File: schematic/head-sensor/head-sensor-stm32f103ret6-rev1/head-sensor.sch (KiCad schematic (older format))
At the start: 11 parts

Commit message: Head sensor schematic in process
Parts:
- added P?: USART1, ~, symbol CONN_4
- added P?: NRF24L01, ~, symbol NRF24L01
- added P?: RFID-RC522-MODULE, ~, symbol RFID-RC522-MODULE
- added P? (x3): CONN_1, ~, symbol CONN_1
- added P?: USART3, ~, symbol CONN_4
- added P?: SensorsIn, ~, symbol CONN_6
- added Q? (x3): MOSFET_N, ~, symbol MOSFET_N
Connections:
- net +3.3V: now also P?.2 (P2), P?.2 (VCC), P?.7 (RST), P?.8 (3.3V)
- net DGND: now also P?.1 (GND), P?.1 (P1), P?.1 (P1), P?.6 (GND)
- net at U?.14 (WKUP/USART2_CTS/ADC123_IN0/TIM2_CH1_ETR/TIM5_CH1/TIM8_ETR/PA0): now also P?.1
- net at U?.15 (USART2_RTS/ADC123_IN1/TIM5_CH2/TIM2_CH2/PA1): now also P?.2
- net at U?.16 (USART2_TX/TIM5_CH3/ADC123_IN2/TIM2_CH3/PA2): now also P?.3
- net at U?.17 (USART2_RX/TIM5_CH4/ADC123_IN3/TIM2_CH4/PA3): now also P?.4
- net at U?.20 (SPI1_NSS/USART2_CK/DAC_OUT1/ADC12_IN4/PA4): now also P?.5
- net at U?.21 (SPI1_SCK/DAC_OUT2/ADC12_IN5/PA5): now also P?.6
- net at U?.22 (SPI1_MISO/TIM8_BKIN/ADC12_IN6/TIM3_CH1/PA6): now also Q?.G
- net at U?.23 (SPI1_MOSI/TIM8_CH1N/ADC12_IN7/TIM3_CH2/PA7): now also Q?.G
- net at U?.26 (ADC12_IN8/TIM3_CH3/TIM8_CH2N/PB0): now also Q?.G
- net at U?.29 (I2C2_SCL/USART3_TX/PB10): now also P?.3 (P3)
- net at U?.30 (I2C2_SDA/USART3_RX/PB11): now also P?.4 (P4)
- net at U?.33 (SPI2_NSS/I2S2_WS/I2C2_SMBA/USART3_CK/TIM1_BKIN/PB12): now also P?.4 (CSN)
- net at U?.34 (SPI2_SCK/I2S2_CK/USART3_CTS/TIM1_CH1N/PB13): now also P?.5 (SCK)
- net at U?.35 (SPI2_MISO/TIM1_CH2N/USART3_RTS/PB14): now also P?.7 (MISO)
- net at U?.36 (SPI2_MOSI/I2S2_SD/TIM1_CH3N/PB15): now also P?.6 (MOSI)
- net at U?.42 (USART1_TX/TIM1_CH2/PA9): now also P?.3 (P3)
- net at U?.43 (USART1_RX/TIM1_CH3/PA10): now also P?.4 (P4)
- net at U?.46 (JTMS/SWDIO/PA13): now also P?.1
- net at U?.49 (JTCK/SWCLK/PA14): now also P?.1
- net at U?.50 (JTDI/SPI3_NSS/I2S3_WS/PA15): now also P?.1 (SDA)
- net at U?.55 (JTDO/SPI3_SCK/I2S3_CK/PB3): now also P?.2 (SCK)
- net at U?.56 (NJTRST/SPI3_MISO/PB4): now also P?.4 (MISO)
- net at U?.57 (I2C1_SMBA/SPI3_MOSI/I2S3_CD/PB5): now also P?.3 (MOSI)
- net at U?.58 (I2C1_SCL/TIM4_CH1/PB6): now also P?.5 (IRQ)
- net at U?.59 (I2C1_SDA/TIM4_CH2/PB7): now also P?.3 (CE)
- net at U?.61 (TIM4_CH3/SDIO_D4/PB8): now also P?.8 (IRQ)
- net at U?.7 (~NRST): now also P?.1
- new net AGND: Q?.S, Q?.S, Q?.S

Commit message: Head sensor schematic in process
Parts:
- added C?: C, ~, symbol C
- added P?: MICROSD-SDIO, ~, symbol MICROSD-SDIO
- added P?: CONN_4, ~, symbol CONN_4
- added P?: CONN_6, ~, symbol CONN_6
- added Q? (x6): MOSFET_N, ~, symbol MOSFET_N
- added R? (x8): R, ~, symbol R
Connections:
- net DGND is gone; now on net AGND: C?.2, C?.2, C?.2, C?.2, C?.2, C?.2, C?.2, P?.1 (GND), P?.1 (P1), P?.1 (P1), P?.6 (GND), U?.12 (VSSA), U?.18 (VSS), U?.31 (VSS), U?.47 (VSS), U?.63 (VSS)
- net GND is gone; now on net AGND: C?.2, U?.1 (GND/Adj)
- net +3.3V: now also C?.2, P?.4 (Vdd), R?.1, R?.2, R?.2, R?.2, R?.2
- net AGND: now also C?.1, P?.6 (GND), Q?.S, Q?.S, Q?.S, Q?.S, Q?.S, Q?.S
- net at U?.10 (PC2/ADC123_IN12): now also Q?.G
- net at U?.11 (PC3/ADC123_IN13): now also Q?.G
- net at U?.24 (PC4/ADC12_IN14): now also Q?.G
- net at U?.25 (PC5/ADC12_IN15): now also Q?.G
- net at U?.39 (PC8/TIM8_CH3/SDIO_D0): now also P?.7 (DAT0), R?.1
- net at U?.40 (PC9/TIM8_CH4/SDIO_D1): now also P?.8 (DAT1/nIRQ), R?.1
- net at U?.51 (PC10/UART4_TX/SDIO_D2): now also P?.1 (DAT2), R?.1
- net at U?.52 (PC11/UART4_RX/SDIO_D3): now also P?.2 (DAT3), R?.1
- net at U?.53 (PC12/UART5_TX/SDIO_CK): now also P?.5 (CLK)
- net at U?.54 (PD2/TIM3_ETR/UART5_RX/SDIO_CMD): now also P?.3 (CMD), R?.2
- net at U?.8 (PC0/ADC123_IN10): now also Q?.G
- net at U?.9 (PC1/ADC123_IN11): now also Q?.G
- net +BATT: now reaches U?.3 (In)
- net at Q?.D: now also R?.1 (x3)
- new net: P?.3 (P3), R?.2
- new net: P?.2 (P2), R?.2
- new net: P?.1 (P1), R?.2
- new net: P?.5, Q?.D
- new net: P?.4, Q?.D
- new net: P?.3, Q?.D
- new net: P?.2, Q?.D
- new net: P?.1, Q?.D
- new net: P?.6, Q?.D
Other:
- moved on the sheet: C?, U?

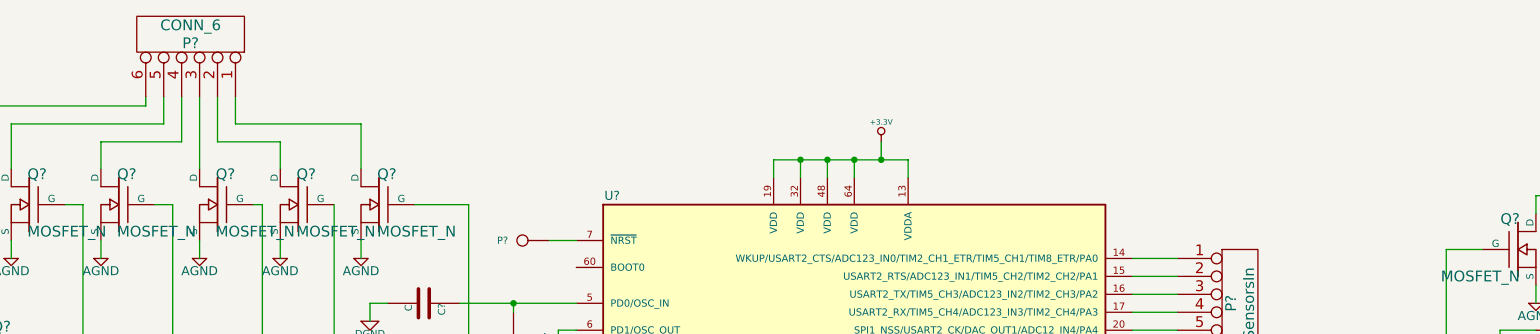
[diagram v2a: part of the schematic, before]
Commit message: Some connectors on scheme
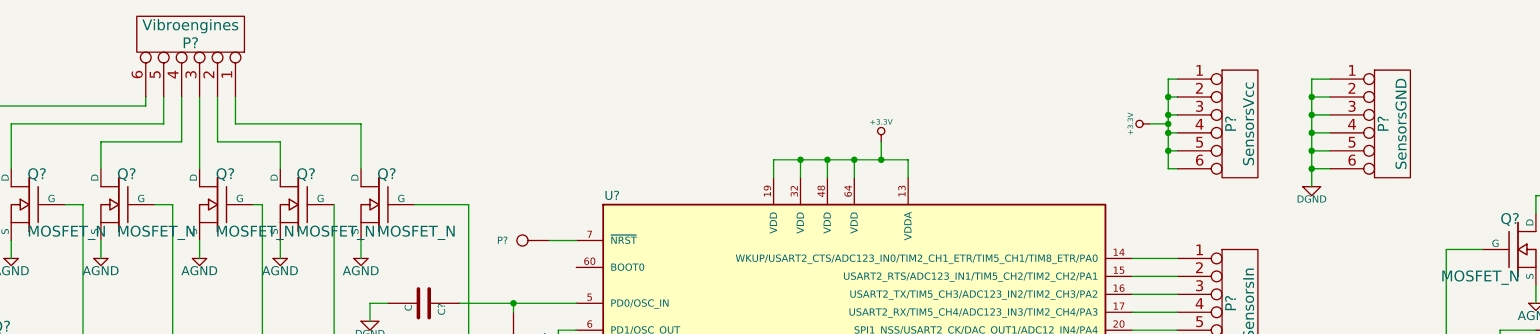
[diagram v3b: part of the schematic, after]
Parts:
- added P?: SensorsVcc, ~, symbol CONN_6
- added P?: SensorsGND, ~, symbol CONN_6
- P?: value CONN_6 -> Vibroengines
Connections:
- net +3.3V: now also P?.1, P?.2, P?.3, P?.4, P?.5, P?.6
- net AGND: now also P?.1, P?.2, P?.3, P?.4, P?.5, P?.6
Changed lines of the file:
@@
 Sheet 1 1
 Title "Lazertag head sensor"
-Date "13 jan 2015"
+Date "14 jan 2015"
 Rev "1"
 Comp ""
@@
 P 1900 700
 F 0 "P?" V 1850 700 60  0000 C CNN
-F 1 "CONN_6" V 1950 700 60  0000 C CNN
+F 1 "Vibroengines" V 1950 700 60  0000 C CNN
 F 2 "~" H 1900 700 60  0000 C CNN
 F 3 "~" H 1900 700 60  0000 C CNN
@@
 	2000 5300 2000 5400
 Connection ~ 2000 5400
+$Comp
+L CONN_6 P?
+U 1 1 54B638F6
+P 7750 1200
+F 0 "P?" V 7700 1200 60  0000 C CNN
+F 1 "SensorsVcc" V 7800 1200 60  0000 C CNN
+F 2 "~" H 7750 1200 60  0000 C CNN
+F 3 "~" H 7750 1200 60  0000 C CNN
+	1    7750 1200
+	1    0    0    -1
+$EndComp
+$Comp
+L CONN_6 P?
+U 1 1 54B63911
+P 8600 1200
+F 0 "P?" V 8550 1200 60  0000 C CNN
+F 1 "SensorsGND" V 8650 1200 60  0000 C CNN
+F 2 "~" H 8600 1200 60  0000 C CNN
+F 3 "~" H 8600 1200 60  0000 C CNN
+	1    8600 1200
+	1    0    0    -1
+$EndComp
+$Comp
+L +3.3V #PWR?
+U 1 1 54B63936
+P 7250 1200
+F 0 "#PWR?" H 7250 1160 30  0001 C CNN
+F 1 "+3.3V" H 7250 1310 30  0000 C CNN
+F 2 "" H 7250 1200 60  0000 C CNN
+F 3 "" H 7250 1200 60  0000 C CNN
+	1    7250 1200
+	0    -1   -1   0
+$EndComp
+Wire Wire Line
+	7400 1450 7350 1450
+Wire Wire Line
+	7350 1450 7350 950
+Wire Wire Line
+	7350 950  7400 950
+Wire Wire Line
+	7400 1050 7350 1050
+Connection ~ 7350 1050
+Wire Wire Line
+	7400 1150 7350 1150
+Connection ~ 7350 1150
+Wire Wire Line
+	7400 1250 7350 1250
+Connection ~ 7350 1250
+Wire Wire Line
+	7400 1350 7350 1350
+Connection ~ 7350 1350
+Wire Wire Line
+	7250 1200 7350 1200
+Connection ~ 7350 1200
+$Comp
+L DGND #PWR?
+U 1 1 54B63F33
+P 8150 1550
+F 0 "#PWR?" H 8150 1550 40  0001 C CNN
+F 1 "DGND" H 8150 1480 40  0000 C CNN
+F 2 "" H 8150 1550 60  0000 C CNN
+F 3 "" H 8150 1550 60  0000 C CNN
+	1    8150 1550
+	1    0    0    -1
+$EndComp
+Wire Wire Line
+	8150 1550 8150 950
+Wire Wire Line
+	8150 950  8250 950
+Wire Wire Line
+	8250 1050 8150 1050
+Connection ~ 8150 1050
+Wire Wire Line
+	8250 1150 8150 1150
+Connection ~ 8150 1150
+Wire Wire Line
+	8250 1250 8150 1250
+Connection ~ 8150 1250
+Wire Wire Line
+	8250 1350 8150 1350
+Connection ~ 8150 1350
+Wire Wire Line
+	8250 1450 8150 1450
+Connection ~ 8150 1450
 $EndSCHEMATC

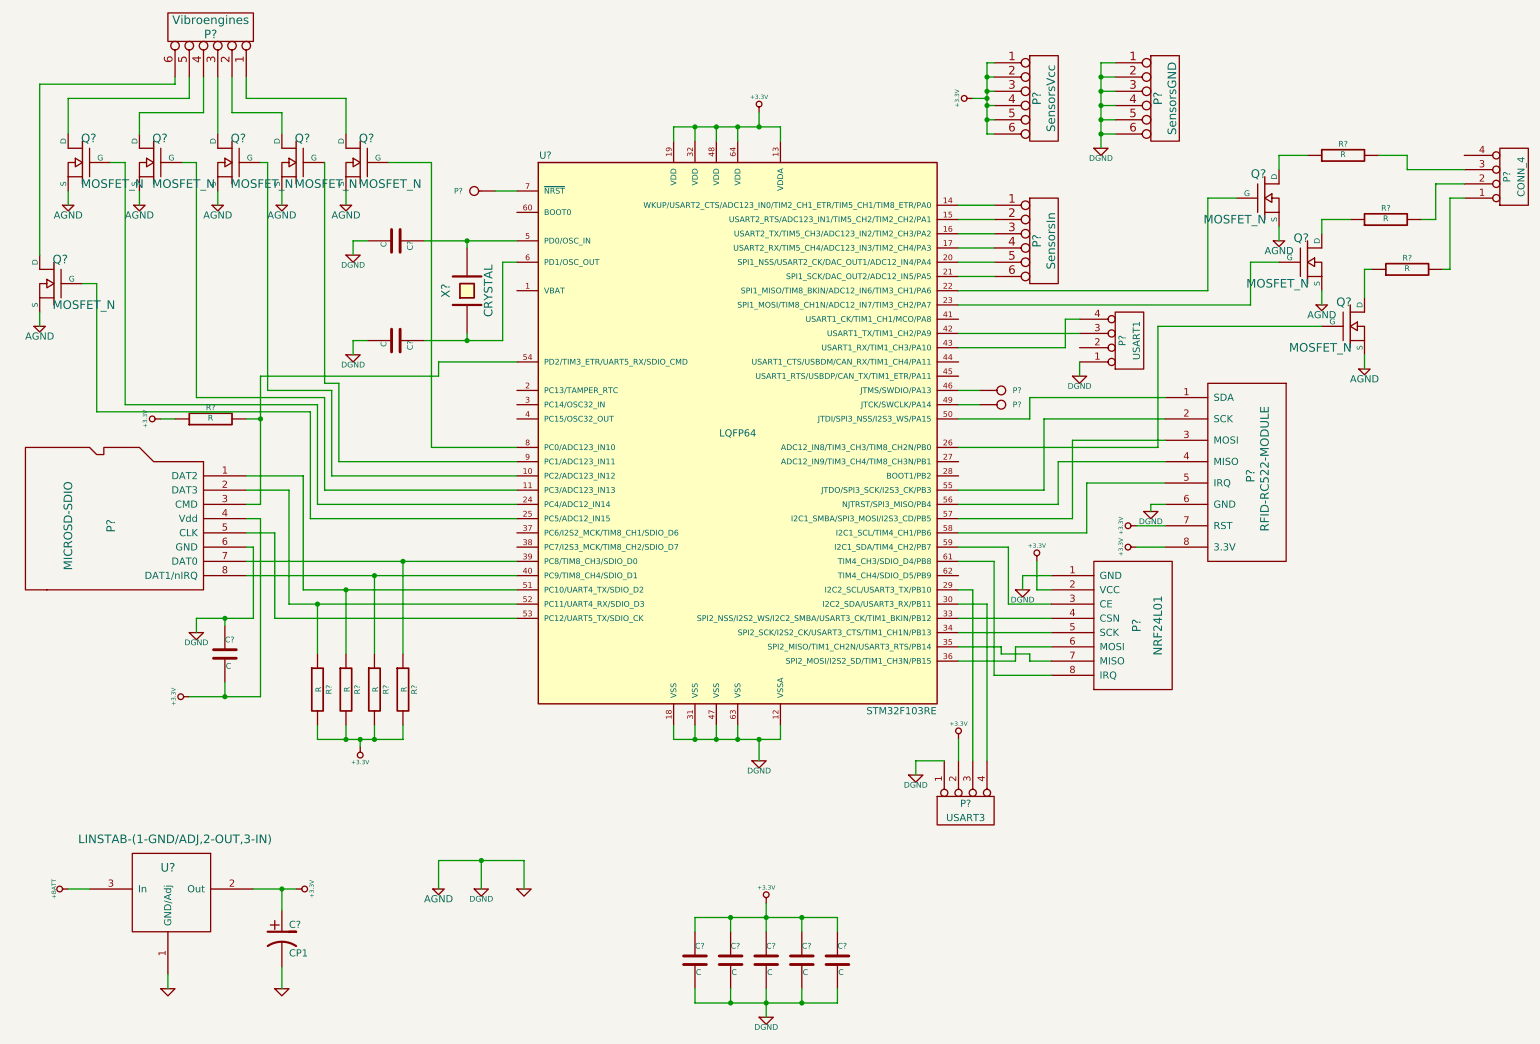
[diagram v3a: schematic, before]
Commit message: head sensor pcb beginned
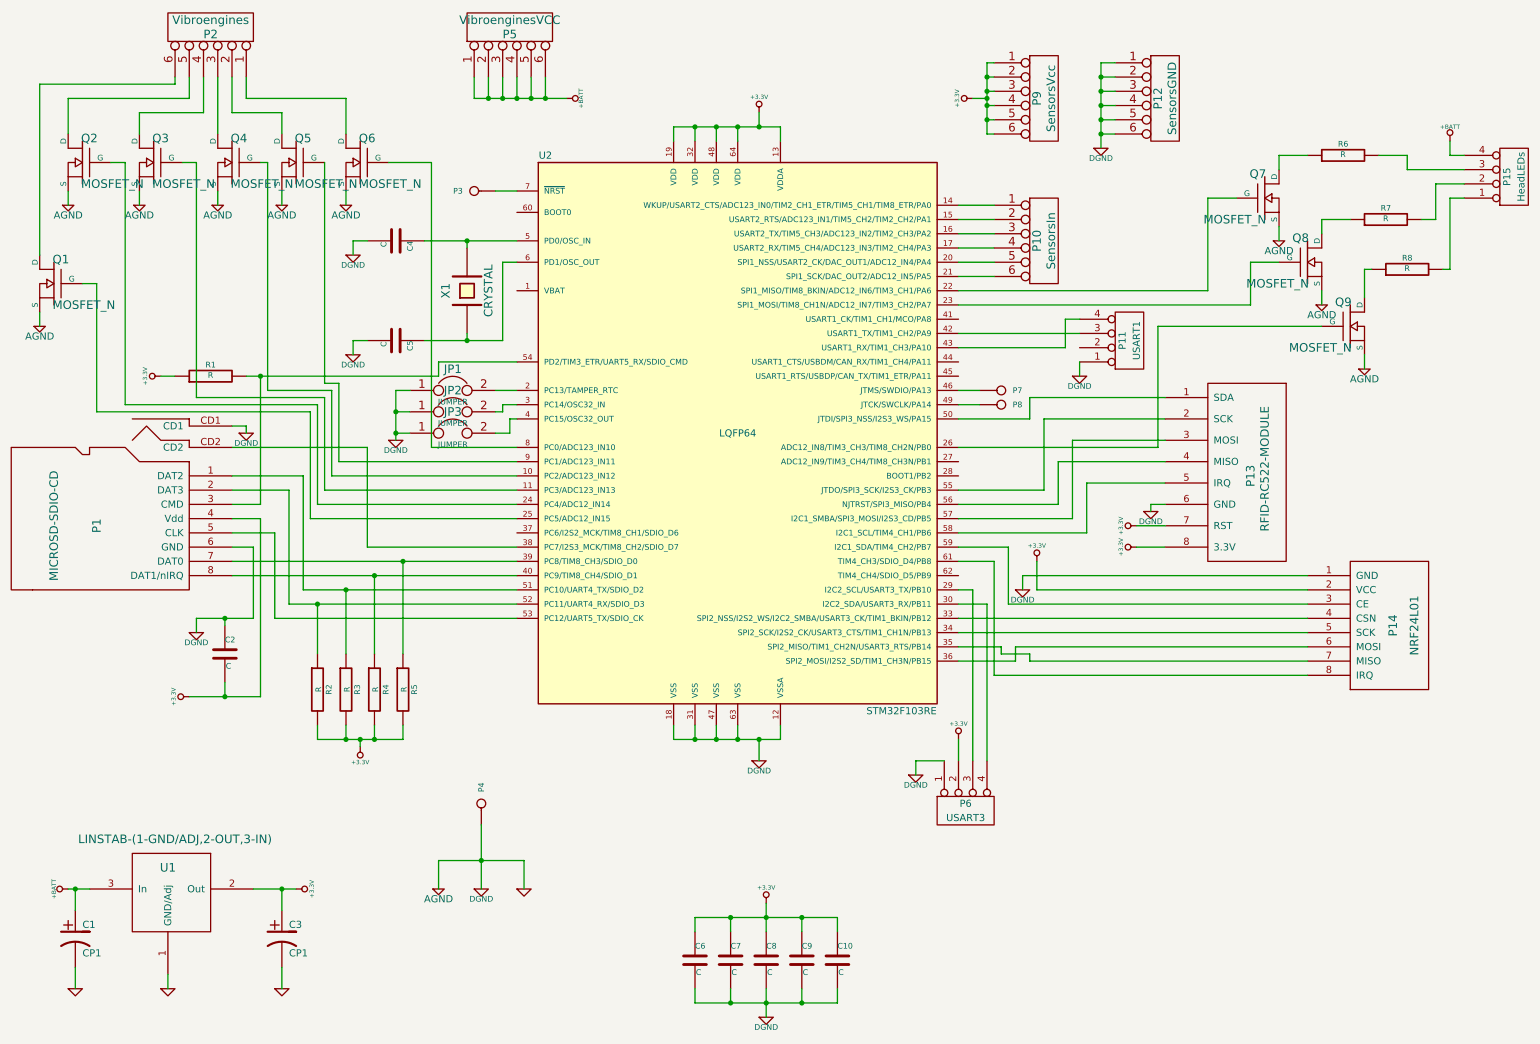
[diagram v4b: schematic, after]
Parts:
- removed P?: MICROSD-SDIO, ~, symbol MICROSD-SDIO
- added C1: CP1, ~, symbol CP1
- added JP1, JP2, JP3: JUMPER, ~, symbol JUMPER
- added P1: MICROSD-SDIO-CD, ~, symbol MICROSD-SDIO-CD
- added P4: SWGND, ~, symbol CONN_1
- added P5: VibroenginesVCC, ~, symbol CONN_6
- P15: renamed from P?; value CONN_4 -> HeadLEDs
- P3: renamed from P?; value CONN_1 -> NRST
- P7: renamed from P?; value CONN_1 -> SWDIO
- P8: renamed from P?; value CONN_1 -> SWCLK
- gave numbers to parts that had none: 37
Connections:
- net +3.3V: now also P1.4 (Vdd)
- net +BATT: now also P15.4 (P4), C1.1, P5.1, P5.2, P5.3, P5.4, P5.5, P5.6
- net AGND: now also C1.2, JP1.1, JP2.1, JP3.1, P1.6 (GND), P1.CD1, P4.1
- net at U2.2 (PC13/TAMPER_RTC): now also JP1.2
- net at U2.3 (PC14/OSC32_IN): now also JP2.2
- net at U2.38 (PC7/I2S3_MCK/TIM8_CH2/SDIO_D7): now also P1.CD2
- net at R5.1, U2.39 (PC8/TIM8_CH3/SDIO_D0): now also P1.7 (DAT0)
- net at U2.4 (PC15/OSC32_OUT): now also JP3.2
- net at R4.1, U2.40 (PC9/TIM8_CH4/SDIO_D1): now also P1.8 (DAT1/nIRQ)
- net at R3.1, U2.51 (PC10/UART4_TX/SDIO_D2): now also P1.1 (DAT2)
- net at R2.1, U2.52 (PC11/UART4_RX/SDIO_D3): now also P1.2 (DAT3)
- net at U2.53 (PC12/UART5_TX/SDIO_CK): now also P1.5 (CLK)
- net at R1.2, U2.54 (PD2/TIM3_ETR/UART5_RX/SDIO_CMD): now also P1.3 (CMD)
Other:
- moved on the sheet: P14, R1

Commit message: head sensor pcb near no be done
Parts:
- added P16: Power, ~, symbol CONN_2
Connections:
- net +BATT: now also P16.2 (PM)
- net AGND: now also P16.1 (P1)
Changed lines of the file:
@@
 Sheet 1 1
 Title "Lazertag head sensor"
-Date "14 jan 2015"
+Date "16 jan 2015"
 Rev "1"
 Comp ""
@@
 Wire Wire Line
 	3000 4350 4050 4350
+$Comp
+L CONN_2 P16
+U 1 1 54B92F5D
+P 8850 6100
+F 0 "P16" V 8800 6100 40  0000 C CNN
+F 1 "Power" V 8900 6100 40  0000 C CNN
+F 2 "~" H 8850 6100 60  0000 C CNN
+F 3 "~" H 8850 6100 60  0000 C CNN
+	1    8850 6100
+	1    0    0    1
+$EndComp
+$Comp
+L AGND #PWR042
+U 1 1 54B92F78
+P 8400 6300
+F 0 "#PWR042" H 8400 6300 40  0001 C CNN
+F 1 "AGND" H 8400 6230 50  0000 C CNN
+F 2 "" H 8400 6300 60  0000 C CNN
+F 3 "" H 8400 6300 60  0000 C CNN
+	1    8400 6300
+	1    0    0    -1
+$EndComp
+Wire Wire Line
+	8400 6300 8400 6200
+Wire Wire Line
+	8400 6200 8500 6200
+Wire Wire Line
+	8400 5800 8400 6000
+Wire Wire Line
+	8400 6000 8500 6000
+$Comp
+L +BATT #PWR?
+U 1 1 54B93397
+P 8400 5800
+F 0 "#PWR?" H 8400 5750 20  0001 C CNN
+F 1 "+BATT" H 8400 5900 30  0000 C CNN
+F 2 "" H 8400 5800 60  0000 C CNN
+F 3 "" H 8400 5800 60  0000 C CNN
+	1    8400 5800
+	1    0    0    -1
+$EndComp
 $EndSCHEMATC
